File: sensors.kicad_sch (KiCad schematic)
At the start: 9 parts, among them IC4 BME690, U2 BMP581, U3 BME280

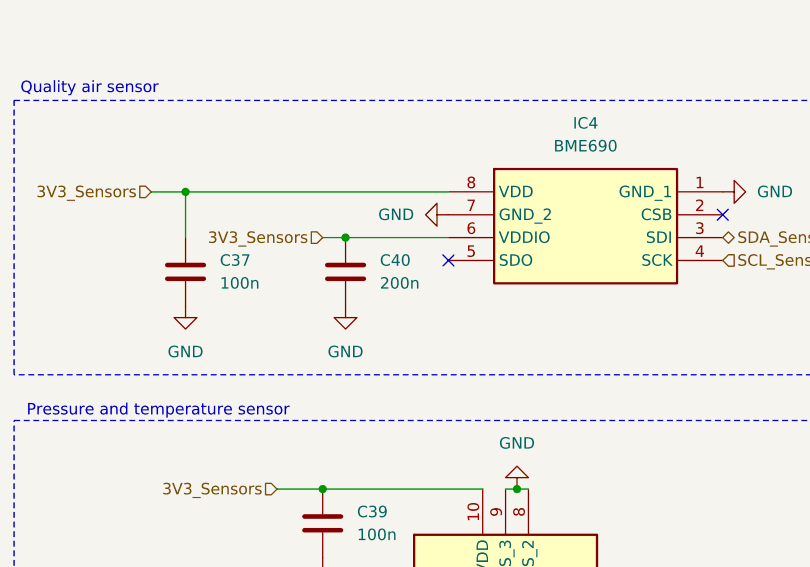
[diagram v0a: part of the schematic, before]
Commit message: Complete all references for components
Modifgy Y1 and Y2 capacitors footprint from 0603 to 0402
Modify footprint of SWD connector
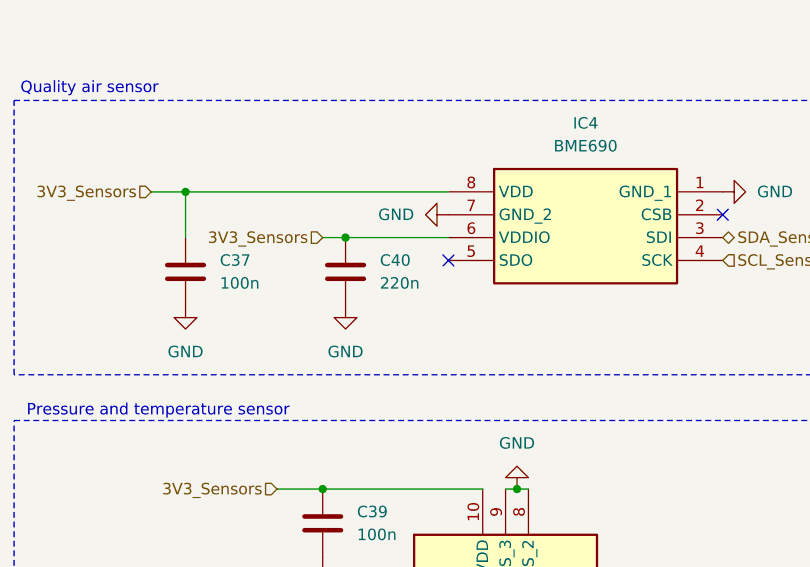
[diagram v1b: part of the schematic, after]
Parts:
- C37, C38, C39, C41, C42: Manufacturer_Name (none) -> Wurth Elektronik; Manufacturer_Part_Number (none) -> 885012206020
- C40: value 200n -> 220n; Manufacturer_Name (none) -> Wurth Elektronik; Manufacturer_Part_Number (none) -> 885012206022
- U3: Manufacturer_Name (none) -> Bosch Sensortec; Manufacturer_Part_Number (none) -> BME280
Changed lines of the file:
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@@
 			)
 		)
-		(property "Datasheet" ""
+		(property "Datasheet" "https://www.we-online.com/components/products/datasheet/885012206020.pdf"
 			(at 218.44 57.15 0)
 			(hide yes)
@@
 		)
 		(property "Description" "Unpolarized capacitor"
+			(at 218.44 57.15 0)
+			(hide yes)
+			(show_name no)
+			(do_not_autoplace no)
+			(effects
+				(font
+					(size 1.27 1.27)
+				)
+			)
+		)
+		(property "Manufacturer_Name" "Wurth Elektronik"
+			(at 218.44 57.15 0)
+			(hide yes)
+			(show_name no)
+			(do_not_autoplace no)
+			(effects
+				(font
+					(size 1.27 1.27)
+				)
+			)
+		)
+		(property "Manufacturer_Part_Number" "885012206020"
 			(at 218.44 57.15 0)
 			(hide yes)
@@
 			)
 		)
-		(property "Datasheet" ""
+		(property "Datasheet" "https://www.we-online.com/components/products/datasheet/885012206020.pdf"
 			(at 81.28 69.85 0)
 			(hide yes)
@@
 		)
 		(property "Description" "Unpolarized capacitor"
+			(at 81.28 69.85 0)
+			(hide yes)
+			(show_name no)
+			(do_not_autoplace no)
+			(effects
+				(font
+					(size 1.27 1.27)
+				)
+			)
+		)
+		(property "Manufacturer_Name" "Wurth Elektronik"
+			(at 81.28 69.85 0)
+			(hide yes)
+			(show_name no)
+			(do_not_autoplace no)
+			(effects
+				(font
+					(size 1.27 1.27)
+				)
+			)
+		)
+		(property "Manufacturer_Part_Number" "885012206020"
 			(at 81.28 69.85 0)
 			(hide yes)
@@
 			)
 		)
-		(property "Value" "200n"
+		(property "Value" "220n"
 			(at 102.87 71.1199 0)
 			(show_name no)
@@
 			)
 		)
-		(property "Datasheet" ""
+		(property "Datasheet" "https://www.we-online.com/components/products/datasheet/885012206022.pdf"
 			(at 99.06 69.85 0)
 			(hide yes)
@@
 		)
 		(property "Description" "Unpolarized capacitor"
+			(at 99.06 69.85 0)
+			(hide yes)
+			(show_name no)
+			(do_not_autoplace no)
+			(effects
+				(font
+					(size 1.27 1.27)
+				)
+			)
+		)
+		(property "Manufacturer_Name" " Wurth Elektronik"
+			(at 99.06 69.85 0)
+			(hide yes)
+			(show_name no)
+			(do_not_autoplace no)
+			(effects
+				(font
+					(size 1.27 1.27)
+				)
+			)
+		)
+		(property "Manufacturer_Part_Number" "885012206022"
 			(at 99.06 69.85 0)
 			(hide yes)
@@
 			)
 		)
+		(property "Manufacturer_Name" "Bosch Sensortec"
+			(at 198.12 69.85 0)
+			(hide yes)
+			(show_name no)
+			(do_not_autoplace no)
+			(effects
+				(font
+					(size 1.27 1.27)
+				)
+			)
+		)
+		(property "Manufacturer_Part_Number" "BME280"
+			(at 198.12 69.85 0)
+			(hide yes)
+			(show_name no)
+			(do_not_autoplace no)
+			(effects
+				(font
+					(size 1.27 1.27)
+				)
+			)
+		)
 		(pin "8"
 		)
@@
 			)
 		)
-		(property "Datasheet" ""
+		(property "Datasheet" "https://www.we-online.com/components/products/datasheet/885012206020.pdf"
 			(at 82.55 115.57 0)
 			(hide yes)
@@
 		)
 		(property "Description" "Unpolarized capacitor"
+			(at 82.55 115.57 0)
+			(hide yes)
+			(show_name no)
+			(do_not_autoplace no)
+			(effects
+				(font
+					(size 1.27 1.27)
+				)
+			)
+		)
+		(property "Manufacturer_Name" "Wurth Elektronik"
+			(at 82.55 115.57 0)
+			(hide yes)
+			(show_name no)
+			(do_not_autoplace no)
+			(effects
+				(font
+					(size 1.27 1.27)
+				)
+			)
+		)
+		(property "Manufacturer_Part_Number" "885012206020"
 			(at 82.55 115.57 0)
 			(hide yes)
@@
 			)
 		)
-		(property "Datasheet" ""
+		(property "Datasheet" "https://www.we-online.com/components/products/datasheet/885012206020.pdf"
 			(at 96.52 97.79 0)
 			(hide yes)
@@
 		)
 		(property "Description" "Unpolarized capacitor"
+			(at 96.52 97.79 0)
+			(hide yes)
+			(show_name no)
+			(do_not_autoplace no)
+			(effects
+				(font
+					(size 1.27 1.27)
+				)
+			)
+		)
+		(property "Manufacturer_Name" "Wurth Elektronik"
+			(at 96.52 97.79 0)
+			(hide yes)
+			(show_name no)
+			(do_not_autoplace no)
+			(effects
+				(font
+					(size 1.27 1.27)
+				)
+			)
+		)
+		(property "Manufacturer_Part_Number" "885012206020"
 			(at 96.52 97.79 0)
 			(hide yes)
@@
 			)
 		)
-		(property "Datasheet" ""
+		(property "Datasheet" "https://www.we-online.com/components/products/datasheet/885012206020.pdf"
 			(at 179.07 57.15 0)
 			(hide yes)
@@
 			(at 179.07 57.15 0)
 			(hide yes)
+			(show_name no)
+			(do_not_autoplace no)
+			(effects
+				(font
+					(size 1.27 1.27)
+				)
+			)
+		)
+		(property "Manufacturer_Name" "Wurth Elektronik"
+			(at 179.07 57.15 0)
+			(hide yes)
+			(show_name no)
+			(do_not_autoplace no)
+			(effects
+				(font
+					(size 1.27 1.27)
+				)
+			)
+		)
+		(property "Manufacturer_Part_Number" "885012206020"
+			(at 179.07 57.15 0)
+			(hide yes)

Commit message: End of BOM
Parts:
- U2: Manufacturer_Name BOSCH -> Bosch Sensortec
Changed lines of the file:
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@@
 			)
 		)
-		(property "Manufacturer_Name" "BOSCH"
+		(property "Manufacturer_Name" "Bosch Sensortec"
 			(at 128.27 796.52 0)
 			(hide yes)

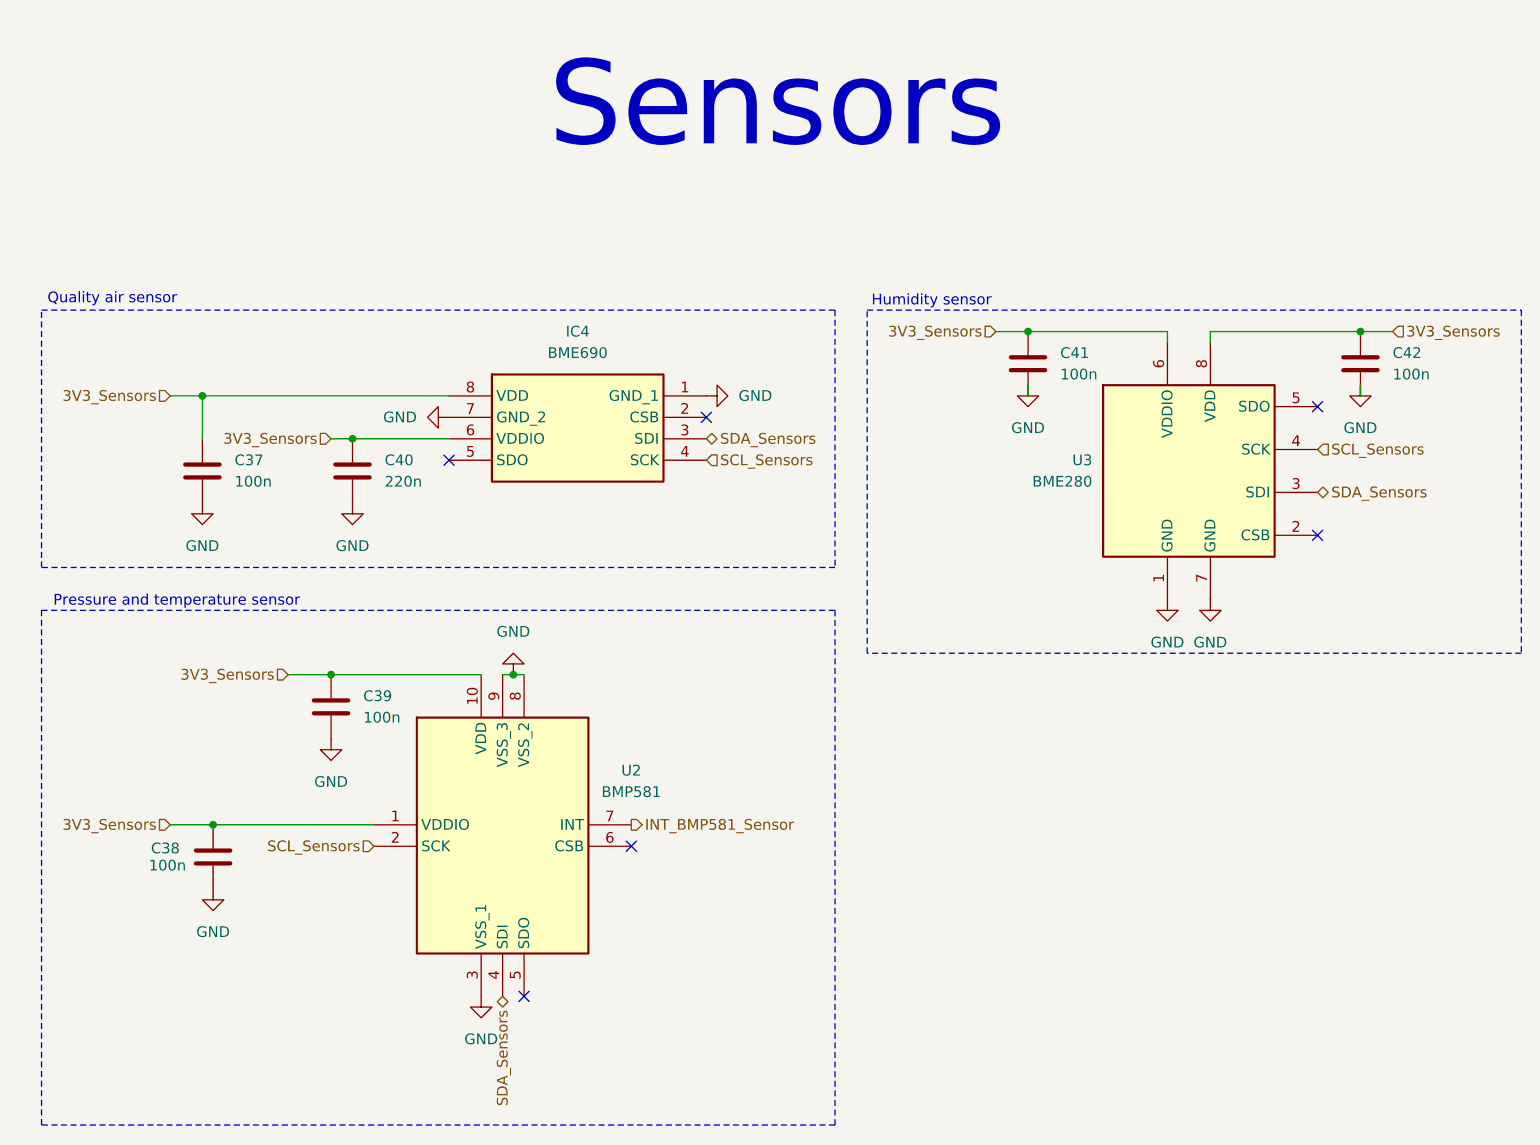
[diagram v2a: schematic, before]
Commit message: Set I2C address for BMP sensors and document address
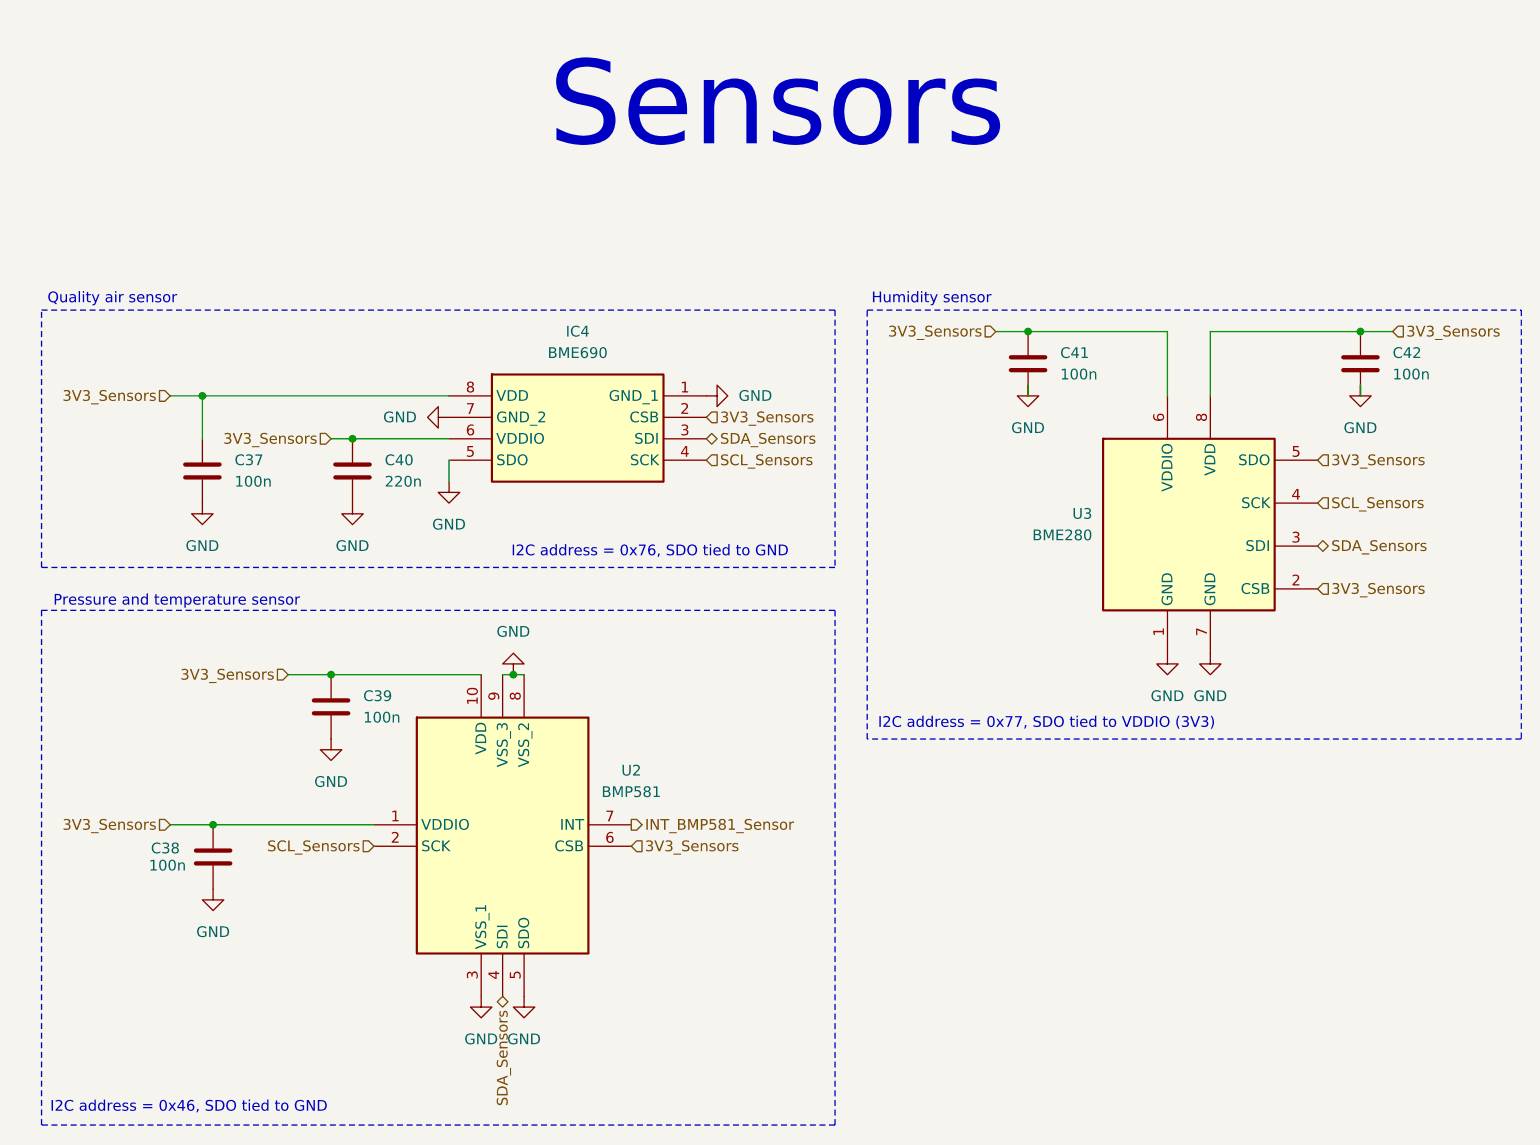
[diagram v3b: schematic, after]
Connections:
- net 3V3_Sensors: now also IC4.2 (CSB), U2.6 (CSB), U3.2 (CSB), U3.5 (SDO)
- net GND: now also IC4.5 (SDO), U2.5 (SDO)
- no-connect marks 6 -> 0
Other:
- note added: "I2C address = 0x46, SDO tied to GND"
- note added: "I2C address = 0x76, SDO tied to GND"
- note added: "I2C address = 0x77, SDO tied to VDDIO (3V3)"
- moved on the sheet: U3
